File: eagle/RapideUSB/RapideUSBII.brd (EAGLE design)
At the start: 50 x 24.6 mm, 39 parts, among them Q1 12MHz

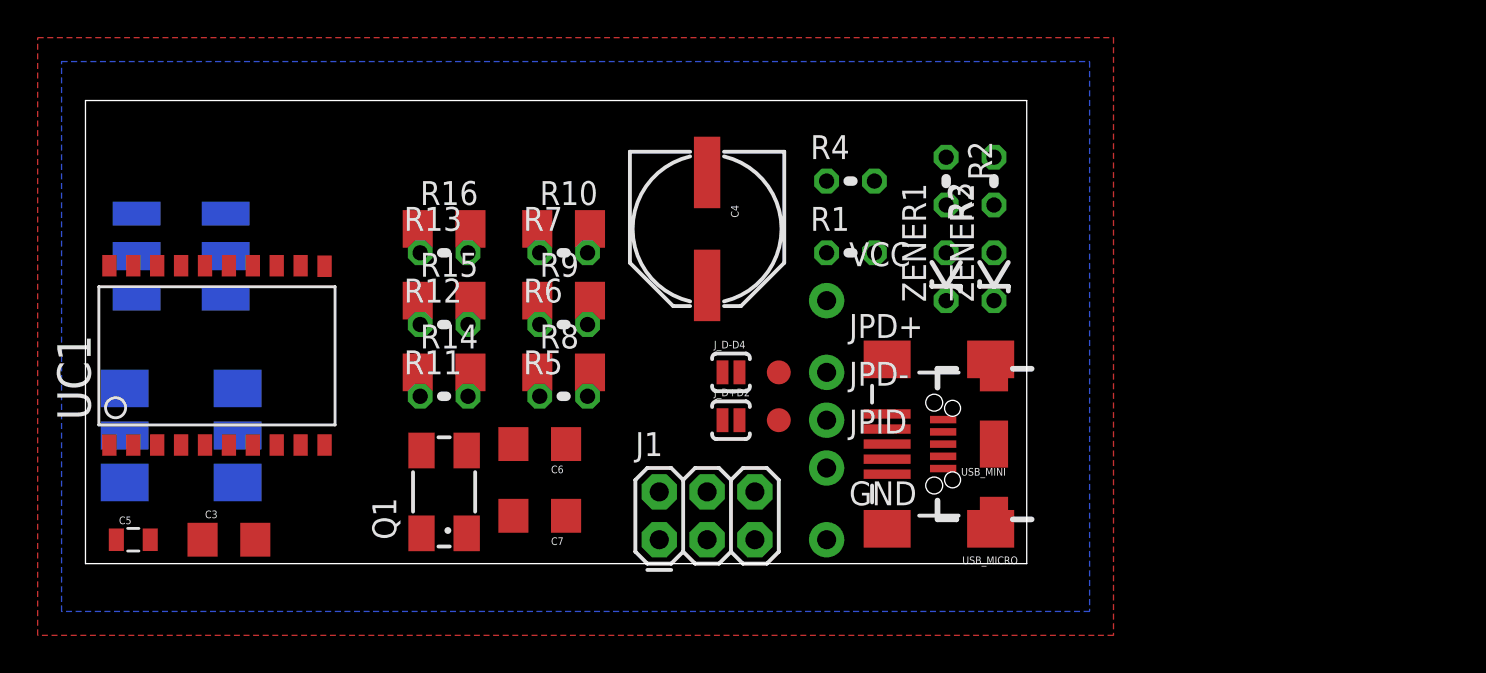
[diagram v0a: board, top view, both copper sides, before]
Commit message: Routed ok, need labelling
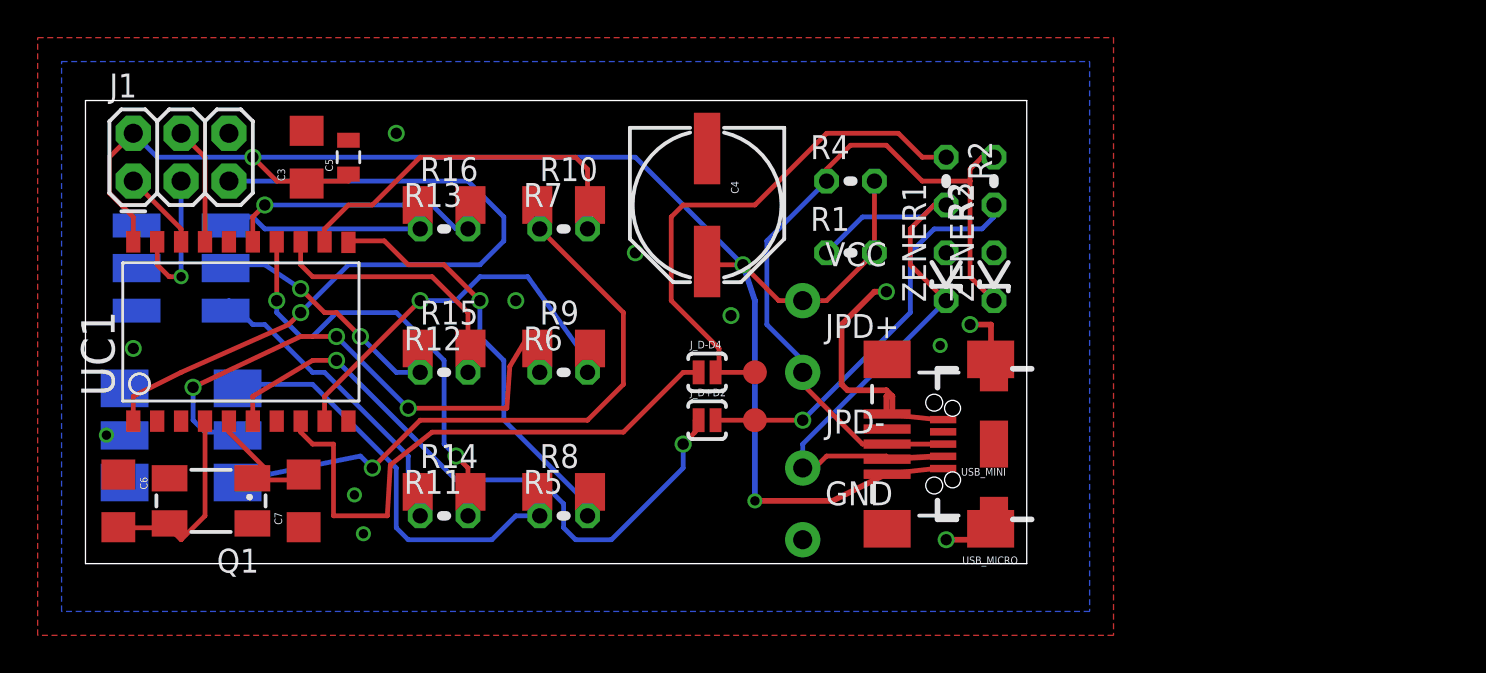
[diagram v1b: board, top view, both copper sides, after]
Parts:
- removed JPID: (no value), SparkFun-Connectors:1X01_NO_SILK
- moved J1 33.8 mm to (2.54, 20.3)
- moved C5 23.3 mm to (14.0, 21.6), turned to 90 degrees
- moved C6 22.6 mm to (1.75, 3.33), turned to 270 degrees
- moved C3 20.7 mm to (11.7, 21.6), turned to 90 degrees
- moved C7 12.6 mm to (11.6, 3.33), turned to 90 degrees
- moved Q1 12.4 mm to (6.67, 3.33), turned to 180 degrees
- moved R11 6.35 mm to (19.1, 2.54)
- moved R5 6.35 mm to (25.4, 2.54)
- moved R14 6.35 mm to (19.1, 3.81)
- moved R8 6.35 mm to (25.4, 3.81)
- moved JPD- 2.84 mm to (38.1, 5.08)
- moved R15 2.54 mm to (19.1, 11.4)
- moved R9 2.54 mm to (25.4, 11.4)
- moved R12 2.54 mm to (19.1, 10.2)
- moved R6 2.54 mm to (25.4, 10.2)
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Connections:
- removed net D5: UC1.9
- removed net D6: UC1.11
- removed net N$13: UC1.12
- removed net N$2: UC1.15
- removed net N$3: UC1.14
- removed net N$4: UC1.13
- net LED1B: now also UC1.12
- net LED1G: now also UC1.11
- net LED1R: now also UC1.9
- net LED2B: now also UC1.15
- net LED2G: now also UC1.14
- net LED2R: now also UC1.13
- net N$14: no longer JPID.1
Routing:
- net VCC: track 0.00 -> 85.7 mm, vias 0 -> 3
- net RESET: track 0.00 -> 40.3 mm, vias 0 -> 1
- net USBD+: track 0.00 -> 40.3 mm
- net N$18: track 0.00 -> 34.3 mm, vias 0 -> 1
- net D2: track 0.00 -> 34.0 mm, vias 0 -> 2
- net USBD-: track 0.00 -> 31.4 mm
- net D4: track 0.00 -> 30.3 mm
- net N$17: track 0.00 -> 29.6 mm, vias 0 -> 3
- net D-: track 0.00 -> 28.4 mm
- net LED2G: track 0.00 -> 23.7 mm, vias 0 -> 2
- net LED1G: track 0.00 -> 23.6 mm, vias 0 -> 1
- net N$15: track 0.00 -> 23.4 mm
- net LED1R: track 0.00 -> 22.2 mm, vias 0 -> 1
- net D+: track 0.00 -> 21.8 mm, vias 0 -> 1
- net GND: track 0.00 -> 21.3 mm, vias 0 -> 12
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
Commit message: Added cam job and continued preparing the board
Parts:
- added U$1: (no value), kalshagar-images:VUSB_LOGO
- moved R12 0.48 mm to (19.1, 9.68)
- moved R13 0.48 mm to (19.1, 17.3)
- moved R6 0.48 mm to (25.4, 9.68)
- moved R7 0.48 mm to (25.4, 17.3)
- moved R11 0.48 mm to (19.1, 2.06)
- moved R5 0.48 mm to (25.4, 2.06)
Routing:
- net LED2G: track 23.7 -> 27.6 mm
- net N$15: track 23.4 -> 24.5 mm
- net LED1R: track 22.2 -> 23.2 mm
- net LED1G: track 23.6 -> 24.5 mm
- net N$19: track 18.3 -> 19.3 mm
- net D2: track 34.0 -> 34.9 mm
- net N$23: track 10.7 -> 10.0 mm
- net LED2B: track 14.9 -> 15.6 mm
- net N$20: track 14.0 -> 14.6 mm
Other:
- board text added: "(R4)"
- board text added: "1-10uF"
- board text added: "100uF"
- board text added: "12MHz"
- board text added: "68ohm"
- board text added: "ATTiny2313"
- board text added: "B1"
- board text added: "B2"
- board text added: "D+"
- board text added: "D+=D2"
- board text added: "D-"
- board text added: "D-=D4"
- board text added: "G1"
- board text added: "G2"
- board text added: "Gnd"
- board text added: "R1"
- board text added: "R1 1.5k"
- board text added: "R2"
- board text added: "Vcc"

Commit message: Before resuming working on RapiedUSBII, a quick commit of whatever I did.
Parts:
- added TP_ID: TEST-POINT3X5, SparkFun-Connectors:PAD.03X.05
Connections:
- net N$14: now also TP_ID.P$1
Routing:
- net N$14: track 0.00 -> 19.3 mm
- net N$4: track 0.00 -> 3.17 mm
- net N$3: track 0.00 -> 2.39 mm
- net USBD+: track 40.3 -> 41.4 mm

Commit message: Before routing
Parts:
- added H1: MOUNT-HOLE2.8, holes:2,8
- added J10: (no value), SparkFun-Connectors:1X08_SMD
- added J2, J4, J5, J6, J7, J8: (no value), SparkFun-Connectors:1X08_NO_SILK
- added J3: (no value), SparkFun-Connectors:1X08_SMD_ALT
- added J9: (no value), SparkFun-Connectors:1X06_NO_SILK
- Q1: device crystal:CTS406 -> SparkFun-Clocks:HC49U
- moved LED2 44.7 mm to (47.0, 18.4), flipped to the top
- moved C5 28.1 mm to (42.1, 21.3), flipped to the bottom
- moved C3 26.4 mm to (38.1, 21.9), flipped to the bottom, turned to 180 degrees
- moved LED1 25.9 mm to (30.5, 8.89)
- moved J_D-D4 24.5 mm to (55.9, 1.27), flipped to the bottom, turned to 90 degrees
- moved JP_D- 23.0 mm to (58.4, 7.62), flipped to the bottom
- moved C6 22.9 mm to (24.6, 3.02), flipped to the bottom, turned to 90 degrees
- moved C7 22.9 mm to (34.4, 3.02), flipped to the bottom, turned to 270 degrees
- moved Q1 22.9 mm to (29.5, 3.02), flipped to the bottom, turned to 0 degrees
- moved J1 22.9 mm to (25.4, 20.3)
- moved U$1 22.9 mm to (51.1, 1.27)
- moved UC1 22.9 mm to (30.5, 12.7)
- moved R10 22.2 mm to (47.0, 14.0)
- moved R7 22.2 mm to (47.0, 12.2)
- moved R13 22.2 mm to (40.6, 12.2)
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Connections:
- net D0: now also J10.8
- net D1: now also J10.7
- net D2: now also J10.6
- net D3: now also J10.5
- net D4: now also J10.4
- net GND: now also J9.1, J9.2, J9.3
- net LED1B: now also J3.8
- net LED1G: now also J10.2
- net LED1R: now also J10.3
- net LED2B: now also J3.5
- net LED2G: now also J3.6
- net LED2R: now also J3.7
- net MISO: now also J3.2
- net MOSI: now also J3.3
- net N$1: now also J3.4
- net N$23: now also Q1.2; no longer Q1.3
- net SCK: now also J3.1
- net VCC: now also J9.4, J9.5, J9.6
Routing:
- net VCC: track 85.7 -> 0.00 mm, vias 3 -> 0
- net USBD+: track 41.4 -> 0.00 mm
- net RESET: track 40.3 -> 0.00 mm, vias 1 -> 0
- net D2: track 34.9 -> 0.00 mm, vias 2 -> 0
- net N$18: track 34.1 -> 0.00 mm, vias 1 -> 0
- net USBD-: track 31.4 -> 0.00 mm
- net D4: track 30.3 -> 0.00 mm
- net N$17: track 30.1 -> 0.00 mm, vias 3 -> 0
- net D-: track 28.4 -> 0.00 mm
- net LED2G: track 27.6 -> 0.00 mm, vias 2 -> 0
- net LED1G: track 24.5 -> 0.00 mm, vias 1 -> 0
- net N$15: track 24.5 -> 0.00 mm
- net LED1R: track 23.2 -> 0.00 mm, vias 1 -> 0
- net D+: track 21.8 -> 0.00 mm, vias 1 -> 0
- net GND: track 21.3 -> 0.00 mm, vias 12 -> 0
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- removed copper zone on layer 1, net GND
- removed copper zone on layer 16, net GND
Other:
- board size 50 x 24.6 mm -> 70 x 24.6 mm
- board text added: "B0"
- board text added: "B7"
- board text added: "D0"
- board text added: "D6"
- board text added: "NC"

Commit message: RapideUSB II sample code checked in.
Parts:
- moved U$1 16.3 mm to (56.8, 16.5), flipped to the bottom
- moved Q1 0.32 mm to (29.5, 3.33), flipped to the top, turned to 180 degrees
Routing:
- net VCC: track 0.00 -> 122.6 mm, vias 0 -> 2
- net GND: track 0.00 -> 91.3 mm, vias 0 -> 6
- net D4: track 0.00 -> 57.7 mm, vias 0 -> 3
- net D2: track 0.00 -> 52.3 mm, vias 0 -> 2
- net USBD+: track 0.00 -> 50.3 mm
- net LED1G: track 0.00 -> 50.2 mm, vias 0 -> 1
- net LED1B: track 0.00 -> 46.9 mm
- net D-: track 0.00 -> 44.4 mm
- net LED2G: track 0.00 -> 44.3 mm, vias 0 -> 2
- net LED2B: track 0.00 -> 38.8 mm, vias 0 -> 3
- net LED1R: track 0.00 -> 36.1 mm, vias 0 -> 2
- net LED2R: track 0.00 -> 36.0 mm, vias 0 -> 2
- net SCK: track 0.00 -> 33.9 mm, vias 0 -> 1
- net USBD-: track 0.00 -> 31.2 mm, vias 0 -> 1
- net N$19: track 0.00 -> 30.2 mm
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- added copper zone on layer 16, net GND
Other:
- board text added: "Id"
- board text added: "Led1"
- board text added: "Led2"
- board text added: "RapideUSB II - v1.0 - Feb 2020"
- board text added: "http://electrogeek.cc/RapideUSB.html"
